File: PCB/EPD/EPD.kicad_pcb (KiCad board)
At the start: 2 copper layers, 70 x 70 mm, 66 parts, among them J1 Conn_01x26, J2 Shelly, J3 USB-PROG, J4 BTN1, J6 BTN2, J7 USB-C-Socket-V, J8 PWR, P1 +, P10 2, P11 1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

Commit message: Missing VBUS!
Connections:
- D6 pad 2: Net-(D6-A) -> VBUS
- J7 pad A4: Net-(D6-A) -> VBUS
- J7 pad A9: Net-(D6-A) -> VBUS
- J7 pad B4: Net-(D6-A) -> VBUS
- J7 pad B9: Net-(D6-A) -> VBUS
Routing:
- net VBUS: track 0.00 -> 20.0 mm, vias 0 -> 3
- net Net-(D6-A): track 13.2 -> 0.00 mm, vias 2 -> 0

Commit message: Smaller
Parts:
- moved D7 22.3 mm to (88.4, 80.1)
- moved C14 7.76 mm to (104.5, 72.6), turned to 90 degrees
- moved C3 7.75 mm to (103.7, 72.6), turned to 90 degrees
- moved C15 7.73 mm to (102.8, 72.6), turned to 90 degrees
- moved C4 7.72 mm to (102.0, 72.6), turned to 90 degrees
- moved C7 7.71 mm to (101.2, 72.6), turned to 90 degrees
- moved C11 7.69 mm to (100.3, 72.6), turned to 90 degrees
- moved C12 7.18 mm to (94.9, 73.0), turned to 180 degrees
- moved R7 6.94 mm to (98.6, 98.4), turned to 180 degrees
- moved C22 4.88 mm to (96.8, 98.4)
- moved C1 4.70 mm to (108.5, 75.0)
- moved C17 3.54 mm to (107.7, 81.8)
- moved P1 3.50 mm to (104.3, 103.8)
- moved P10 3.50 mm to (95.0, 103.8)
- moved P11 3.50 mm to (90.7, 103.8)
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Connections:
- U4 pad 9: unconnected-(U4-GPIO5-Pad9) -> GND
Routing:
- net BTN2: track 6.06 -> 30.3 mm, vias 0 -> 2
- net +3.3V: track 96.0 -> 77.5 mm, vias 4 -> 3
- net BTN1: track 8.86 -> 25.8 mm, vias 0 -> 2
- net Net-(J4-Pin_2): track 10.8 -> 24.8 mm, vias 0 -> 1
- net GND: track 28.3 -> 37.8 mm, vias 28 -> 17
- net Net-(J1-Pin_24): track 1.91 -> 8.15 mm
- net Net-(D3-K): track 12.9 -> 18.6 mm
- net Net-(D1-A): track 7.06 -> 12.6 mm
- net Net-(J1-Pin_18): track 2.24 -> 7.17 mm
- net VBUS: track 20.0 -> 24.5 mm
- net Net-(J1-Pin_20): track 2.34 -> 6.69 mm
- net Net-(J1-Pin_5): track 2.41 -> 6.72 mm
- net Net-(J1-Pin_22): track 2.26 -> 6.40 mm
- net Net-(J6-Pin_2): track 13.2 -> 17.2 mm, vias 0 -> 2
- net PWR: track 22.5 -> 18.9 mm
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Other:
- board text removed: "+"
- board text removed: "-"
- board text removed: "EPD driver"

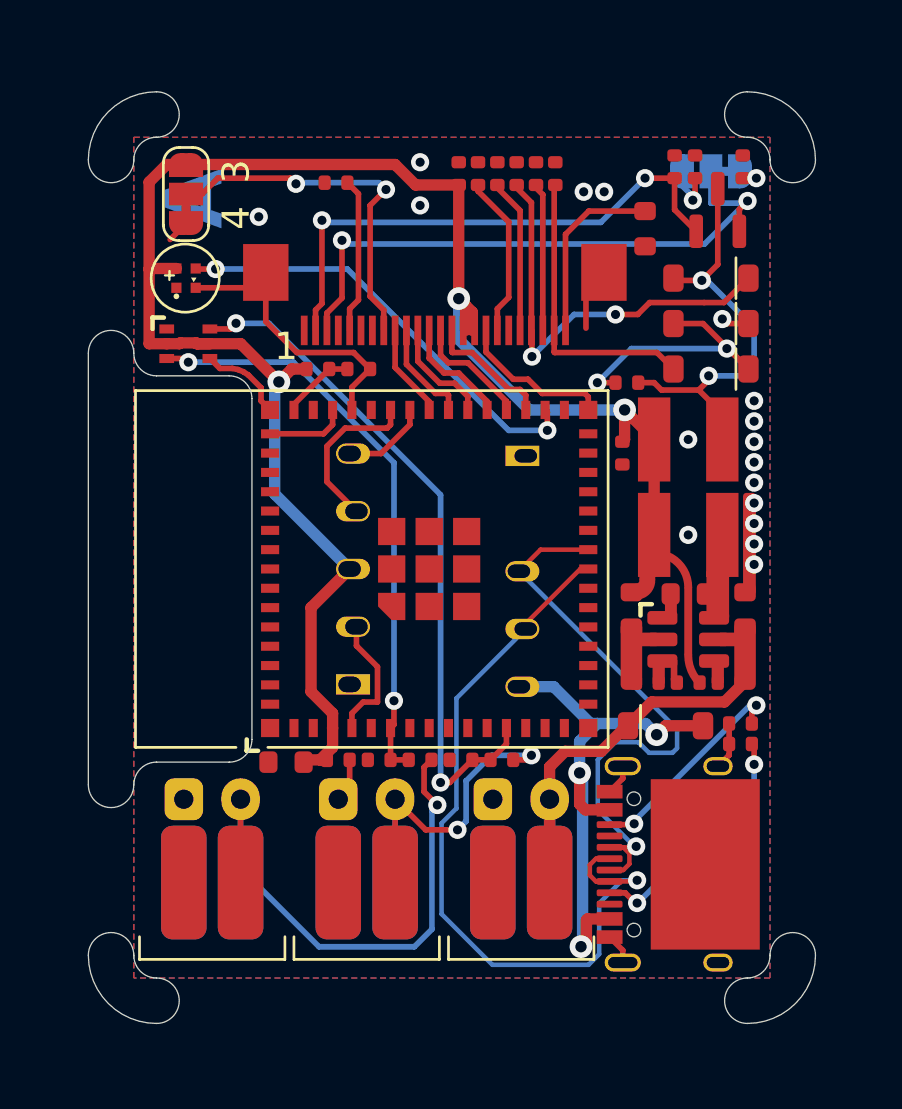
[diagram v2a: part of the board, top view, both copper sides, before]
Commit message: FPC centred and retracked
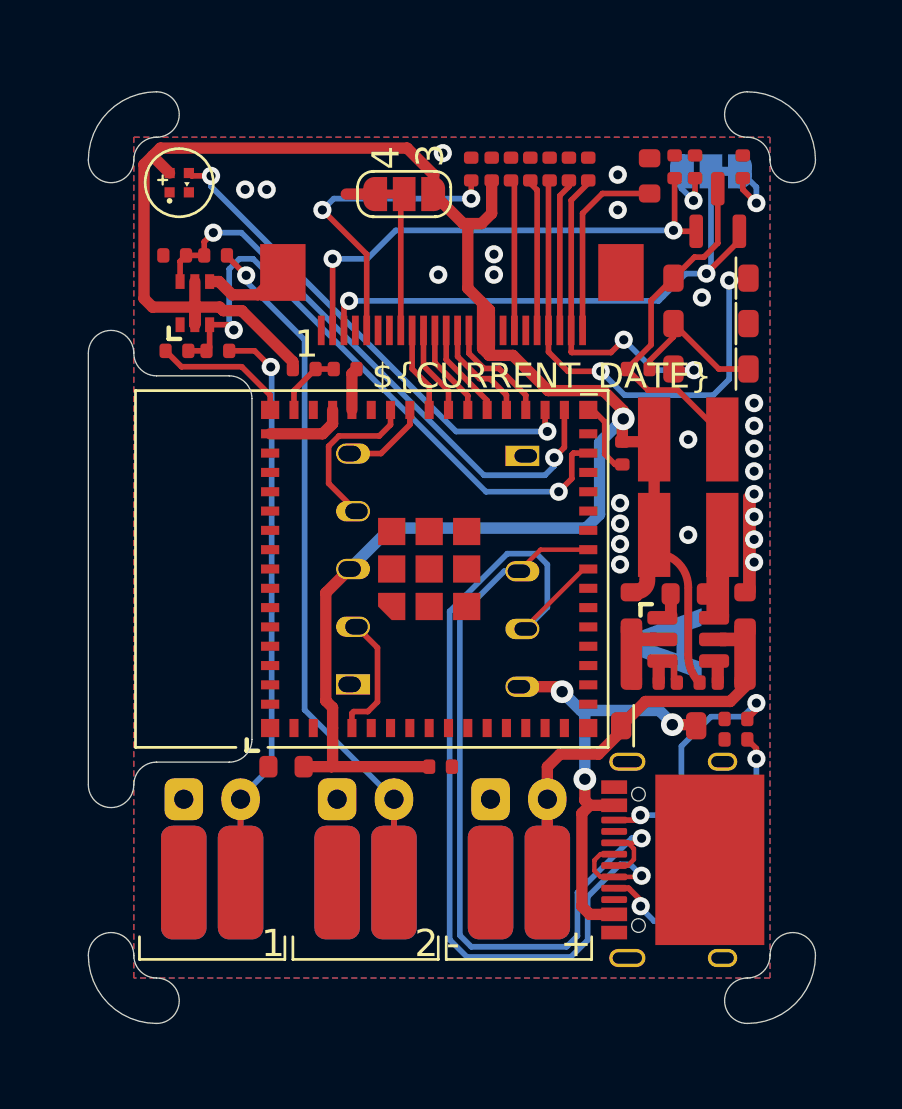
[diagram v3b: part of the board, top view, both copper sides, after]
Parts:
- moved C21 25.5 mm to (87.8, 76.2)
- moved R6 25.5 mm to (89.6, 76.2)
- moved C22 20.1 mm to (87.9, 80.4)
- moved R7 20.1 mm to (89.7, 80.4)
- moved JP2 9.60 mm to (97.9, 73.5), turned to 0 degrees
- moved C12 5.98 mm to (100.8, 72.4), turned to 90 degrees
- moved C2 4.51 mm to (99.5, 98.7)
- moved D4 4.21 mm to (88.0, 73.0)
- moved C1 2.33 mm to (108.7, 72.7), turned to 90 degrees
- moved D7 1.81 mm to (88.7, 78.3), turned to 90 degrees
- moved C11 1.46 mm to (101.8, 72.4)
- moved C14 1.46 mm to (106.0, 72.4)
- moved C15 1.46 mm to (104.3, 72.4)
- moved C3 1.46 mm to (105.2, 72.4)
- moved C4 1.46 mm to (103.5, 72.4)
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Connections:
- U4 pad 12: BTN2 -> unconnected-(U4-GPIO8-Pad12)
- U4 pad 29: unconnected-(U4-GPIO34-Pad29) -> BTN1
- U4 pad 31: unconnected-(U4-GPIO35-Pad31) -> BTN2
- U4 pad 6: BTN1 -> unconnected-(U4-GPIO2-Pad6)
- U4 pad 9: GND -> unconnected-(U4-GPIO5-Pad9)
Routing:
- net GND: track 37.8 -> 19.6 mm, vias 17 -> 23
- net Net-(J6-Pin_2): track 17.2 -> 34.3 mm, vias 2 -> 1
- net +3.3V: track 77.5 -> 90.6 mm, vias 3 -> 1
- net Net-(J1-Pin_8): track 16.1 -> 5.85 mm, vias 2 -> 0
- net D+: track 26.4 -> 36.0 mm
- net D-: track 33.9 -> 42.3 mm
- net Net-(J1-Pin_5): track 6.72 -> 13.7 mm, vias 0 -> 2
- net Net-(D1-A): track 12.6 -> 6.56 mm, vias 2 -> 0
- net BTN2: track 30.3 -> 25.5 mm
- net Net-(J4-Pin_2): track 24.8 -> 29.0 mm
- net VBUS: track 24.5 -> 21.2 mm
- net Net-(J7-CC1): track 10.6 -> 13.7 mm
- net Net-(D3-K): track 18.6 -> 21.6 mm
- net Net-(J1-Pin_3): track 27.5 -> 24.7 mm
- net RGB: track 19.3 -> 21.7 mm
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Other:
- board text added: "+"
- board text added: "-"
- board text added: "34"
- board text added: "35"
- board text removed: "8"

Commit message: Curvy tracks
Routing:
- net D-: track 42.3 -> 48.1 mm
- net VBUS: track 21.2 -> 24.4 mm
- net Net-(D3-K): track 21.6 -> 22.8 mm
- net Net-(J7-CC1): track 13.7 -> 14.6 mm
- net D+: track 36.0 -> 36.8 mm
- net +3.3V: track 90.6 -> 91.3 mm
- net Net-(J1-Pin_3): track 24.7 -> 24.1 mm
- net Net-(D3-A): track 15.2 -> 15.7 mm

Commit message: BTN added
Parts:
- turned JP1 to 0 degrees
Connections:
- R1 pad 1: Net-(JP1-A) -> Net-(JP1-B)
- R2 pad 2: Net-(JP1-B) -> Net-(JP1-A)
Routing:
- net Net-(JP1-B): track 2.59 -> 3.19 mm
- net Net-(JP1-A): track 3.19 -> 2.59 mm

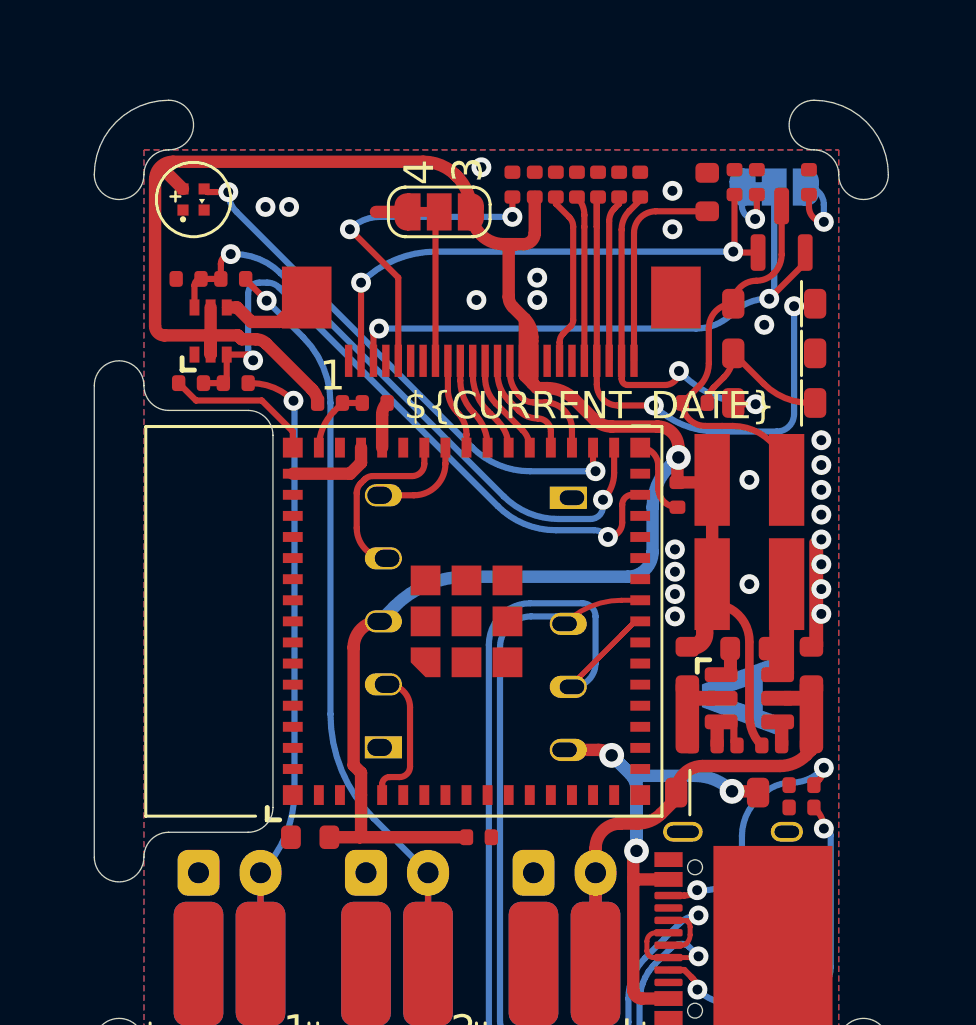
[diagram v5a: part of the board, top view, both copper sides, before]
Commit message: Moved connector for less slack
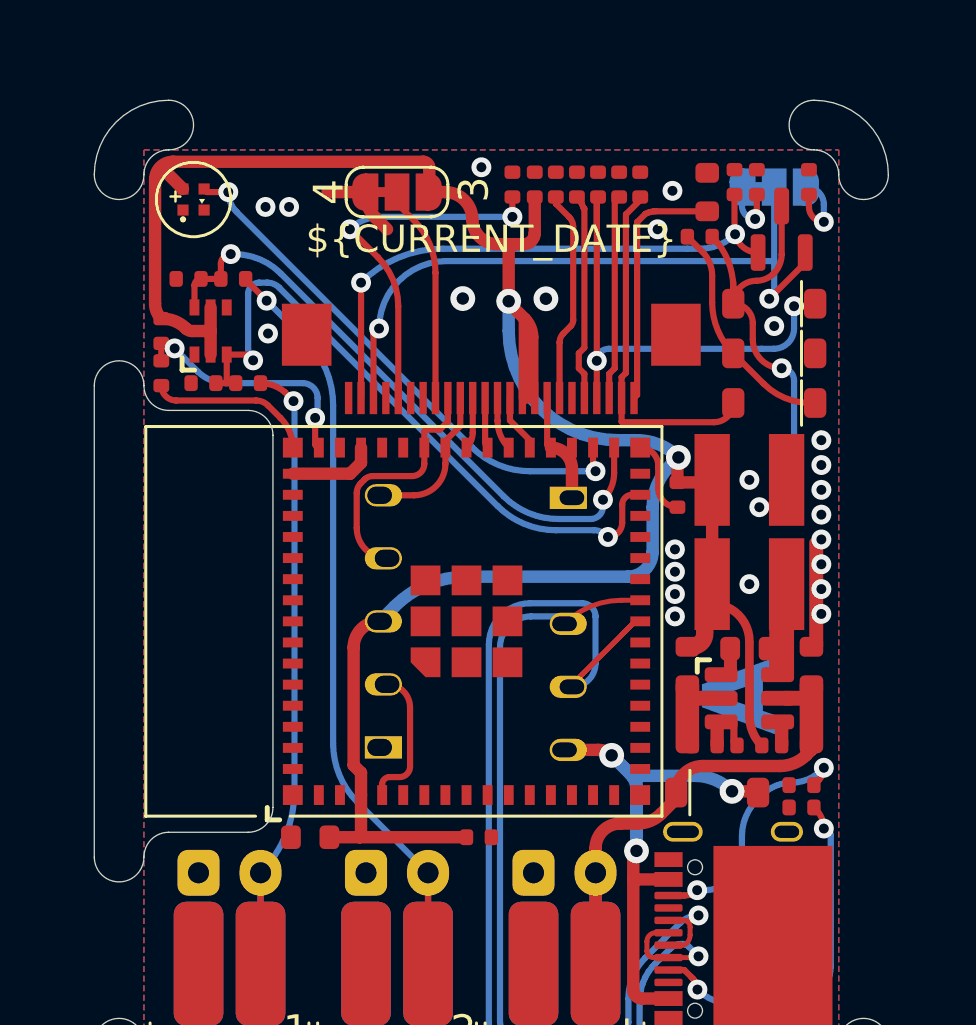
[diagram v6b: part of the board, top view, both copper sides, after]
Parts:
- moved C6 8.68 mm to (86.7, 80.0), turned to -90 degrees
- moved R3 7.39 mm to (86.7, 78.3), turned to -90 degrees
- moved C17 6.70 mm to (108.4, 74.5), turned to 180 degrees
- moved JP2 1.88 mm to (96.2, 72.7)
- moved J1 1.50 mm to (100.0, 79.7)
- moved C22 0.50 mm to (88.4, 80.4)
- moved R7 0.50 mm to (90.2, 80.4)
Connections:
- J2 pad 4: Net-(J2-Rx) -> BUSY
- J2 pad 5: Net-(J2-Tx) -> RST
- U4 pad 33: MOSI -> GND
- U4 pad 34: CLK -> GND
- U4 pad 35: CS -> MOSI
- U4 pad 36: DC -> CLK
- U4 pad 37: RST -> CS
- U4 pad 38: BUSY -> DC
- U4 pad 39: Net-(J2-Tx) -> RST
- U4 pad 40: Net-(J2-Rx) -> BUSY
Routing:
- net Net-(J2-Rx): track 7.29 -> 0.00 mm
- net Net-(U4-EN): track 2.89 -> 10.0 mm, vias 0 -> 2
- net BUSY: track 3.69 -> 10.0 mm
- net Net-(D3-A): track 15.7 -> 20.7 mm, vias 0 -> 2
- net Net-(J2-Tx): track 3.97 -> 0.00 mm
- net Net-(D3-K): track 22.8 -> 19.6 mm
- net Net-(J1-Pin_8): track 5.85 -> 8.80 mm
- net Net-(D1-A): track 6.33 -> 9.26 mm
- net Net-(J1-Pin_3): track 24.1 -> 26.9 mm
- net MOSI: track 5.01 -> 2.33 mm
- net +3.3V: track 91.3 -> 88.7 mm, vias 1 -> 2
- net CLK: track 4.59 -> 2.11 mm
- net RST: track 3.78 -> 6.22 mm
- net CS: track 4.13 -> 2.03 mm
- net DC: track 3.93 -> 2.06 mm
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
